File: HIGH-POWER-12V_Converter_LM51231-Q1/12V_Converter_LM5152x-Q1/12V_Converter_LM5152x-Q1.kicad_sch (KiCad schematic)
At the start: 30 parts, among them M1 60V, M2 CSD18540Q5B, U1 LM51521QRGRRQ1

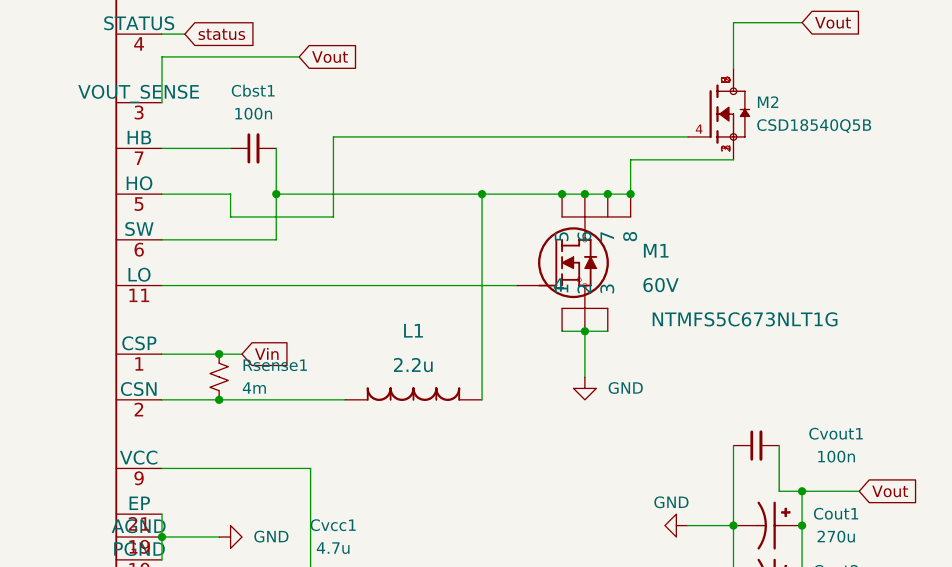
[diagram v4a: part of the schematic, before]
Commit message: updated high power to reflect changes described in review notes
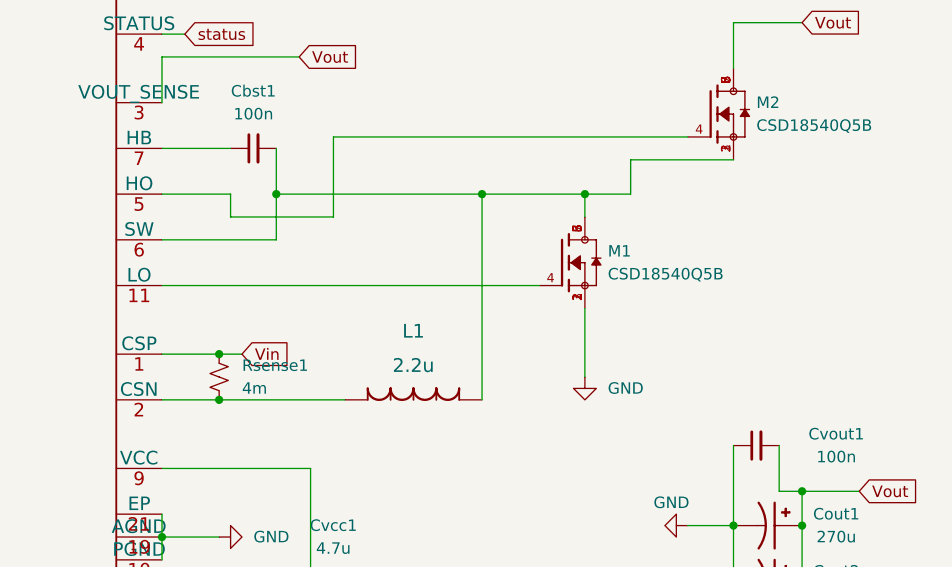
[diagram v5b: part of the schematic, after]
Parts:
- removed M1: 60V, M1:TRANS_NVMFS5834NLWFT1G, symbol N-MOS:SIR826ADP-T1-GE3
- added M1: CSD18540Q5B, M2:TRANS_CSD18540Q5B, symbol M2:CSD18540Q5B
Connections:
- net GND: now also M1.1, M1.2, M1.3
- net at Cbst1.2, L1.1, M2.1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: now also M1.5, M1.6, M1.7, M1.8
- net at U1.11 (LO): now also M1.4
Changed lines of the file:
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@@
   (junction (at 243.84 143.51) (diameter 0) (color 0 0 0 0)
   )
-  (junction (at 224.79 77.47) (diameter 0) (color 0 0 0 0)
-  )
-  (junction (at 227.33 77.47) (diameter 0) (color 0 0 0 0)
-  )
   (junction (at 187.96 77.47) (diameter 0) (color 0 0 0 0)
   )
@@
   (junction (at 246.38 110.49) (diameter 0) (color 0 0 0 0)
   )
+  (junction (at 88.9 86.36) (diameter 0) (color 0 0 0 0)
+  )
+  (junction (at 238.76 120.65) (diameter 0) (color 0 0 0 0)
+  )
+  (junction (at 243.84 132.08) (diameter 0) (color 0 0 0 0)
+  )
+  (junction (at 238.76 151.13) (diameter 0) (color 0 0 0 0)
+  )
+  (junction (at 243.84 128.27) (diameter 0) (color 0 0 0 0)
+  )
+  (junction (at 243.84 147.32) (diameter 0) (color 0 0 0 0)
+  )
+  (junction (at 88.9 93.98) (diameter 0) (color 0 0 0 0)
+  )
+  (junction (at 87.63 48.26) (diameter 0) (color 0 0 0 0)
+  )
+  (junction (at 110.49 97.79) (diameter 0) (color 0 0 0 0)
+  )
+  (junction (at 110.49 53.34) (diameter 0) (color 0 0 0 0)
+  )
+  (junction (at 243.84 139.7) (diameter 0) (color 0 0 0 0)
+  )
+  (junction (at 191.77 120.65) (diameter 0) (color 0 0 0 0)
+  )
+  (junction (at 106.68 118.11) (diameter 0) (color 0 0 0 0)
+  )
+  (junction (at 88.9 88.9) (diameter 0) (color 0 0 0 0)
+  )
+  (junction (at 238.76 147.32) (diameter 0) (color 0 0 0 0)
+  )
+  (junction (at 238.76 135.89) (diameter 0) (color 0 0 0 0)
+  )
+  (junction (at 238.76 128.27) (diameter 0) (color 0 0 0 0)
+  )
+  (junction (at 181.61 100.33) (diameter 0) (color 0 0 0 0)
+  )
   (junction (at 222.25 77.47) (diameter 0) (color 0 0 0 0)
   )
-  (junction (at 88.9 86.36) (diameter 0) (color 0 0 0 0)
-  )
-  (junction (at 238.76 120.65) (diameter 0) (color 0 0 0 0)
-  )
-  (junction (at 243.84 132.08) (diameter 0) (color 0 0 0 0)
-  )
-  (junction (at 238.76 151.13) (diameter 0) (color 0 0 0 0)
-  )
-  (junction (at 243.84 128.27) (diameter 0) (color 0 0 0 0)
-  )
-  (junction (at 243.84 147.32) (diameter 0) (color 0 0 0 0)
-  )
-  (junction (at 88.9 93.98) (diameter 0) (color 0 0 0 0)
-  )
-  (junction (at 87.63 48.26) (diameter 0) (color 0 0 0 0)
-  )
-  (junction (at 110.49 97.79) (diameter 0) (color 0 0 0 0)
-  )
-  (junction (at 110.49 53.34) (diameter 0) (color 0 0 0 0)
-  )
-  (junction (at 243.84 139.7) (diameter 0) (color 0 0 0 0)
-  )
-  (junction (at 191.77 120.65) (diameter 0) (color 0 0 0 0)
-  )
-  (junction (at 106.68 118.11) (diameter 0) (color 0 0 0 0)
-  )
-  (junction (at 88.9 88.9) (diameter 0) (color 0 0 0 0)
-  )
-  (junction (at 238.76 147.32) (diameter 0) (color 0 0 0 0)
-  )
-  (junction (at 238.76 135.89) (diameter 0) (color 0 0 0 0)
-  )
-  (junction (at 238.76 128.27) (diameter 0) (color 0 0 0 0)
-  )
-  (junction (at 181.61 100.33) (diameter 0) (color 0 0 0 0)
-  )
-  (junction (at 219.71 77.47) (diameter 0) (color 0 0 0 0)
-  )
   (junction (at 246.38 120.65) (diameter 0) (color 0 0 0 0)
   )
@@
   (junction (at 175.26 115.57) (diameter 0) (color 0 0 0 0)
   )
-  (junction (at 222.25 92.71) (diameter 0) (color 0 0 0 0)
-  )
   (junction (at 246.38 114.3) (diameter 0) (color 0 0 0 0)
   )
@@
   (junction (at 105.41 48.26) (diameter 0) (color 0 0 0 0)
   )
-  (wire (pts (xy 224.79 77.47) (xy 227.33 77.47))
+  (wire (pts (xy 210.82 77.47) (xy 222.25 77.47))
     (stroke (width 0) (type default) (color 0 0 0 0))
   )
@@
     (stroke (width 0) (type default) (color 0 0 0 0))
   )
-  (wire (pts (xy 222.25 92.71) (xy 222.25 97.79))
+  (wire (pts (xy 222.25 90.17) (xy 222.25 97.79))
     (stroke (width 0) (type default) (color 0 0 0 0))
   )
@@
     (stroke (width 0) (type default) (color 0 0 0 0))
   )
+  (wire (pts (xy 222.25 77.47) (xy 222.25 80.01))
+    (stroke (width 0) (type default) (color 0 0 0 0))
+  )
   (wire (pts (xy 238.76 105.41) (xy 238.76 114.3))
     (stroke (width 0) (type default) (color 0 0 0 0))
@@
     (stroke (width 0) (type default) (color 0 0 0 0))
   )
-  (wire (pts (xy 175.26 87.63) (xy 214.63 87.63))
+  (wire (pts (xy 222.25 77.47) (xy 227.33 77.47))
+    (stroke (width 0) (type default) (color 0 0 0 0))
+  )
+  (wire (pts (xy 175.26 87.63) (xy 217.17 87.63))
     (stroke (width 0) (type default) (color 0 0 0 0))
   )
@@
     (stroke (width 0) (type default) (color 0 0 0 0))
   )
-  (wire (pts (xy 219.71 77.47) (xy 222.25 77.47))
-    (stroke (width 0) (type default) (color 0 0 0 0))
-  )
   (wire (pts (xy 107.95 97.79) (xy 110.49 97.79))
     (stroke (width 0) (type default) (color 0 0 0 0))
@@
     (stroke (width 0) (type default) (color 0 0 0 0))
   )
-  (wire (pts (xy 219.71 92.71) (xy 222.25 92.71))
-    (stroke (width 0) (type default) (color 0 0 0 0))
-  )
   (wire (pts (xy 243.84 105.41) (xy 243.84 110.49))
     (stroke (width 0) (type default) (color 0 0 0 0))
@@
     (stroke (width 0) (type default) (color 0 0 0 0))
   )
-  (wire (pts (xy 210.82 77.47) (xy 219.71 77.47))
-    (stroke (width 0) (type default) (color 0 0 0 0))
-  )
   (wire (pts (xy 96.52 123.19) (xy 96.52 113.03))
     (stroke (width 0) (type default) (color 0 0 0 0))
@@
     (stroke (width 0) (type default) (color 0 0 0 0))
   )
-  (wire (pts (xy 222.25 77.47) (xy 224.79 77.47))
-    (stroke (width 0) (type default) (color 0 0 0 0))
-  )
   (wire (pts (xy 238.76 151.13) (xy 238.76 154.94))
     (stroke (width 0) (type default) (color 0 0 0 0))
@@
   )
   (wire (pts (xy 175.26 115.57) (xy 175.26 118.11))
-    (stroke (width 0) (type default) (color 0 0 0 0))
-  )
-  (wire (pts (xy 222.25 92.71) (xy 224.79 92.71))
     (stroke (width 0) (type default) (color 0 0 0 0))
   )
@@
     (pin "1")
     (pin "2")
-  )
-  (symbol (lib_id "N-MOS:SIR826ADP-T1-GE3") (at 214.63 87.63 0) (unit 1)
-    (in_bom yes) (on_board yes)
-    (property "Reference" "M1" (id 0) (at 228.6 83.82 0)
-      (effects (font (size 1.524 1.524)) (justify left))
-    )
-    (property "Value" "60V" (id 1) (at 228.6 87.63 0)
-      (effects (font (size 1.524 1.524)) (justify left))
-    )
-    (property "Footprint" "M1:TRANS_NVMFS5834NLWFT1G" (id 2) (at 226.06 91.694 0)
-      (effects (font (size 1.524 1.524)) hide)
-    )
-    (property "Datasheet" "NTMFS5C673NLT1G" (id 3) (at 240.03 91.44 0)
-      (effects (font (size 1.524 1.524)))
-    )
-    (property "LCSC" "C5334421" (id 4) (at 214.63 87.63 0)
-      (effects (font (size 1.27 1.27)) hide)
-    )
-    (pin "1")
-    (pin "2")
-    (pin "3")
-    (pin "4")
-    (pin "5")
-    (pin "6")
-    (pin "7")
-    (pin "8")
   )
   (symbol (lib_id "Device:C_Small") (at 194.31 120.65 90) (unit 1)
@@
     (pin "2")
   )
+  (symbol (lib_id "M2:CSD18540Q5B") (at 219.71 85.09 0) (unit 1)
+    (in_bom yes) (on_board yes) (fields_autoplaced)
+    (property "Reference" "M1" (id 0) (at 224.79 83.8199 0)
+      (effects (font (size 1.27 1.27)) (justify left))
+    )
+    (property "Value" "CSD18540Q5B" (id 1) (at 224.79 86.3599 0)
+      (effects (font (size 1.27 1.27)) (justify left))
+    )
+    (property "Footprint" "M2:TRANS_CSD18540Q5B" (id 2) (at 219.71 85.09 0)
+      (effects (font (size 1.27 1.27)) (justify bottom) hide)
+    )
+    (property "Datasheet" "" (id 3) (at 219.71 85.09 0)
+      (effects (font (size 1.27 1.27)) hide)
+    )
+    (property "MANUFACTURER" "Texas Instruments" (id 4) (at 219.71 85.09 0)
+      (effects (font (size 1.27 1.27)) (justify bottom) hide)
+    )
+    (property "PARTREV" "B" (id 5) (at 219.71 85.09 0)
+      (effects (font (size 1.27 1.27)) (justify bottom) hide)
+    )
+    (property "STANDARD" "Manufacturer recommendations" (id 6) (at 219.71 85.09 0)
+      (effects (font (size 1.27 1.27)) (justify bottom) hide)
+    )
+    (property "MAXIMUM_PACKAGE_HEIGHT" "1.05mm" (id 7) (at 219.71 85.09 0)
+      (effects (font (size 1.27 1.27)) (justify bottom) hide)
+    )
+    (pin "1")
+    (pin "2")
+    (pin "3")
+    (pin "4")
+    (pin "5")
+    (pin "6")
+    (pin "7")
+    (pin "8")
+  )
   (symbol (lib_id "Device:C_Small") (at 95.25 88.9 90) (unit 1)
     (in_bom yes) (on_board yes) (fields_autoplaced)
@@
       (reference "L1") (unit 1) (value "2.2u") (footprint "inductor2.2:IHLP6767GZER2R2M51")
     )
-    (path "/64391f12-acdd-4367-a4b2-5a471753d256"
-      (reference "M1") (unit 1) (value "60V") (footprint "M1:TRANS_NVMFS5834NLWFT1G")
+    (path "/d55f5413-9da1-4bb6-b9da-54af2085eaca"
+      (reference "M1") (unit 1) (value "CSD18540Q5B") (footprint "M2:TRANS_CSD18540Q5B")
     )
     (path "/8eae0b44-4011-424d-acfe-3d644836614d"

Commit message: literally not a clue what i did i think i made some gerber files or smth
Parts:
- Cbias1: LCSC C92759 -> C513775
- Cbst1: LCSC C92759 -> C30926
- Ccomp1: LCSC (none) -> C5186918
- Ccomp2: LCSC C107111 -> C1716
- Cin1, Cin2, Coutx1, Coutx2, Coutx3, Coutx4, Coutx5, Coutx6, Coutx7, Coutx8: LCSC C77093 -> C13585
- Cinx1: LCSC C2172920 -> C513775
- Css1: LCSC (none) -> C327005
- Cvcc1: LCSC (none) -> C69335
- Cvout1: LCSC C2842861 -> C30926
- Cvref1: LCSC C85979 -> C107092
- M1, M2: LCSC (none) -> C2863985
- Rcomp1: LCSC C273789 -> C203395
- Rsense1: value 4m -> 3m; LCSC (none) -> C2941089
- Rt1: LCSC C844171 -> C23184
- Rvrefb1: LCSC C165742 -> C23089
- Rvreft1: LCSC C844784 -> C12447
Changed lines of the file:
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@@
       (effects (font (size 1.27 1.27)) hide)
     )
-    (property "LCSC" "C2842861" (id 4) (at 241.3 105.41 90)
+    (property "LCSC" "C30926" (id 4) (at 241.3 105.41 90)
       (effects (font (size 1.27 1.27)) hide)
     )
@@
       (effects (font (size 1.27 1.27)) hide)
     )
-    (property "LCSC" "C85979" (id 4) (at 101.6 113.03 90)
+    (property "LCSC" "C107092" (id 4) (at 101.6 113.03 90)
       (effects (font (size 1.27 1.27)) hide)
     )
@@
       (effects (font (size 1.27 1.27)) hide)
     )
-    (property "LCSC" "C165742" (id 4) (at 106.68 120.65 0)
+    (property "LCSC" "C23089" (id 4) (at 106.68 120.65 0)
       (effects (font (size 1.27 1.27)) hide)
     )
@@
       (effects (font (size 1.27 1.27)) hide)
     )
-    (property "LCSC" "C77093" (id 4) (at 241.3 132.08 90)
+    (property "LCSC" "C13585" (id 4) (at 241.3 132.08 90)
       (effects (font (size 1.27 1.27)) hide)
     )
@@
       (effects (font (size 1.27 1.27)) hide)
     )
-    (property "LCSC" "C77093" (id 4) (at 241.3 128.27 90)
+    (property "LCSC" "C13585" (id 4) (at 241.3 128.27 90)
       (effects (font (size 1.27 1.27)) hide)
     )
@@
       (effects (font (size 1.27 1.27)) hide)
     )
-    (property "LCSC" "C77093" (id 4) (at 241.3 151.13 90)
+    (property "LCSC" "C13585" (id 4) (at 241.3 151.13 90)
       (effects (font (size 1.27 1.27)) hide)
     )
@@
       (effects (font (size 1.27 1.27)) hide)
     )
-    (property "LCSC" "C92759" (id 4) (at 110.49 50.8 0)
+    (property "LCSC" "C513775" (id 4) (at 110.49 50.8 0)
       (effects (font (size 1.27 1.27)) hide)
     )
@@
       (effects (font (size 1.27 1.27)) hide)
     )
-    (property "LCSC" "C844784" (id 4) (at 106.68 115.57 0)
+    (property "LCSC" "C12447" (id 4) (at 106.68 115.57 0)
       (effects (font (size 1.27 1.27)) hide)
     )
@@
       (effects (font (size 1.27 1.27)) hide)
     )
-    (property "LCSC" "C77093" (id 4) (at 241.3 147.32 90)
+    (property "LCSC" "C13585" (id 4) (at 241.3 147.32 90)
       (effects (font (size 1.27 1.27)) hide)
     )
@@
       (effects (font (size 1.27 1.27)) hide)
     )
-    (property "LCSC" "C92759" (id 4) (at 185.42 72.39 90)
+    (property "LCSC" "C30926" (id 4) (at 185.42 72.39 90)
       (effects (font (size 1.27 1.27)) hide)
     )
@@
     )
     (property "Datasheet" "~" (id 3) (at 194.31 120.65 0)
+      (effects (font (size 1.27 1.27)) hide)
+    )
+    (property "LCSC" "C69335" (id 4) (at 194.31 120.65 90)
       (effects (font (size 1.27 1.27)) hide)
     )
@@
       (effects (font (size 1.27 1.27)) hide)
     )
-    (property "LCSC" "C77093" (id 4) (at 241.3 143.51 90)
+    (property "LCSC" "C13585" (id 4) (at 241.3 143.51 90)
       (effects (font (size 1.27 1.27)) hide)
     )
@@
       (effects (font (size 1.27 1.27)) hide)
     )
-    (property "LCSC" "C2172920" (id 4) (at 97.79 50.8 0)
+    (property "LCSC" "C513775" (id 4) (at 97.79 50.8 0)
       (effects (font (size 1.27 1.27)) hide)
     )
@@
       (effects (font (size 1.27 1.27)) hide)
     )
+    (property "LCSC" "C5186918" (id 4) (at 95.25 97.79 90))
     (pin "1")
     (pin "2")
@@
     (property "MAXIMUM_PACKAGE_HEIGHT" "1.05mm" (id 7) (at 236.22 68.58 0)
       (effects (font (size 1.27 1.27)) (justify bottom) hide)
+    )
+    (property "LCSC" "C2863985" (id 8) (at 236.22 68.58 0)
+      (effects (font (size 1.27 1.27)) hide)
     )
     (pin "1")
@@
       (effects (font (size 1.27 1.27)) hide)
     )
-    (property "LCSC" "C77093" (id 4) (at 87.63 50.8 0)
+    (property "LCSC" "C13585" (id 4) (at 87.63 50.8 0)
       (effects (font (size 1.27 1.27)) hide)
     )
@@
       (effects (font (size 1.27 1.27)) hide)
     )
-    (property "LCSC" "C273789" (id 4) (at 105.41 97.79 90)
+    (property "LCSC" "C203395" (id 4) (at 105.41 97.79 90)
       (effects (font (size 1.27 1.27)) hide)
     )
@@
       (effects (font (size 1.27 1.27)) hide)
     )
-    (property "LCSC" "C77093" (id 4) (at 241.3 139.7 90)
+    (property "LCSC" "C13585" (id 4) (at 241.3 139.7 90)
       (effects (font (size 1.27 1.27)) hide)
     )
@@
       (effects (font (size 1.27 1.27)) hide)
     )
-    (property "LCSC" "C77093" (id 4) (at 77.47 50.8 0)
+    (property "LCSC" "C13585" (id 4) (at 77.47 50.8 0)
       (effects (font (size 1.27 1.27)) hide)
     )
@@
       (effects (font (size 1.27 1.27)) hide)
     )
-    (property "LCSC" "C77093" (id 4) (at 241.3 154.94 90)
+    (property "LCSC" "C13585" (id 4) (at 241.3 154.94 90)
       (effects (font (size 1.27 1.27)) hide)
     )
@@
     (property "MAXIMUM_PACKAGE_HEIGHT" "1.05mm" (id 7) (at 219.71 85.09 0)
       (effects (font (size 1.27 1.27)) (justify bottom) hide)
+    )
+    (property "LCSC" "C2863985" (id 8) (at 219.71 85.09 0)
+      (effects (font (size 1.27 1.27)) hide)
     )
     (pin "1")
@@
       (effects (font (size 1.27 1.27)) hide)
     )
-    (property "LCSC" "C107111" (id 4) (at 95.25 88.9 90)
+    (property "LCSC" "C1716" (id 4) (at 95.25 88.9 90)
       (effects (font (size 1.27 1.27)) hide)
     )
@@
       (effects (font (size 1.27 1.27)) hide)
     )
-    (property "LCSC" "C844171" (id 4) (at 111.76 82.55 90)
+    (property "LCSC" "C23184" (id 4) (at 111.76 82.55 90)
       (effects (font (size 1.27 1.27)) hide)
     )
@@
       (effects (font (size 1.27 1.27)) (justify left))
     )
-    (property "Value" "4m" (id 1) (at 184.15 99.0599 0)
+    (property "Value" "3m" (id 1) (at 184.15 99.0599 0)
       (effects (font (size 1.27 1.27)) (justify left))
     )
@@
     )
     (property "Datasheet" "~" (id 3) (at 181.61 97.79 0)
+      (effects (font (size 1.27 1.27)) hide)
+    )
+    (property "LCSC" "C2941089" (id 4) (at 181.61 97.79 0)
       (effects (font (size 1.27 1.27)) hide)
     )
@@
       (effects (font (size 1.27 1.27)) hide)
     )
-    (property "LCSC" "C77093" (id 4) (at 241.3 135.89 90)
+    (property "LCSC" "C13585" (id 4) (at 241.3 135.89 90)
       (effects (font (size 1.27 1.27)) hide)
     )
@@
       (effects (font (size 1.27 1.27)) hide)
     )
+    (property "LCSC" "C327005" (id 4) (at 104.14 86.36 90)
+      (effects (font (size 1.27 1.27)) hide)
+    )
     (pin "1")
     (pin "2")
@@
     )
     (path "/f04dae45-04a1-41bc-a92b-f0b4763478d9"
-      (reference "Rsense1") (unit 1) (value "4m") (footprint "Resistor_SMD:R_2512_6332Metric")
+      (reference "Rsense1") (unit 1) (value "3m") (footprint "Resistor_SMD:R_2512_6332Metric")
     )
     (path "/ea5e4be9-b927-4fca-aab6-cbde3c564ee8"
